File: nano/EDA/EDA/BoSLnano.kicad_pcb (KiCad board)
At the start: 4 copper layers, 74 x 30 mm, 59 parts, among them J1 Micro_SD_Card, J2 Conn_02x04_Counter_Clockwise, J3 Barrel_Jack_Switch, J4 USB_B_Micro, SW1 SPST, U1 MCP1700-3302E_SOT23, U10 FT232RQ, U2 ATmega328P-MMH, U3 MSQA6V1W5T2G, U4 NT3H2111W0FTT, U5 SIM7090, U6 74LV1T34GXH, U7 74LV1T34GXH, U8 MCP7940N-xSN, U9 74HC126PW-Q100, Y1 8 MHz, Y2 32.768 kHz

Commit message: finished bom and schematic - nano
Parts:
- removed BT1: Battery_Cell, SIMFootprints:2996TR
- removed D5, D6: LED, LED_SMD:LED_0603_1608Metric
- removed TP1: PWR_KEY, TestPoint:TestPoint_Pad_D1.0mm
- removed TP2: VDD_EXT, TestPoint:TestPoint_Pad_D1.0mm
- removed TP3: USB_DM, TestPoint:TestPoint_Pad_D1.0mm
- removed TP4: USB_DP, TestPoint:TestPoint_Pad_D1.0mm
- removed TP5: USB_VBUS, TestPoint:TestPoint_Pad_D1.0mm
- removed TP6: BOOT_CFG, TestPoint:TestPoint_Pad_D1.0mm
- removed U10: FT232RQ, Package_DFN_QFN:QFN-32-1EP_5x5mm_P0.5mm_EP3.1x3.1mm
- removed U7: 74LV1T34GXH, SIMFootprints:SOT1226
- removed U8: MCP7940N-xSN, Package_DFN_QFN:DFN-8-1EP_3x2mm_P0.5mm_EP1.3x1.5mm
- removed U9: 74HC126PW-Q100, Package_SO:TSSOP-14_4.4x5mm_P0.65mm
- removed Y2: 32.768 kHz, Crystal:Crystal_SMD_EuroQuartz_EQ161-2Pin_3.2x1.5mm
- added C13: 15 pF, Capacitor_SMD:C_0402_1005Metric, F.Cu at (133.2, 86.6)
- added C14: 1 μF, Capacitor_SMD:C_0402_1005Metric, F.Cu at (156.5, 94.6)
- added C15: 100 nF, Capacitor_SMD:C_0402_1005Metric, F.Cu at (128.7, 83.7)
- added C16: 15 pF, Capacitor_SMD:C_0402_1005Metric, F.Cu at (132.3, 97.1)
- added C17: 220 pF, Capacitor_SMD:C_0402_1005Metric, F.Cu at (135.2, 97.1)
- added C18: 100 nF, Capacitor_SMD:C_0402_1005Metric, F.Cu at (138.2, 95.6)
- added C19: 1 nF, Capacitor_SMD:C_0402_1005Metric, F.Cu at (150.8, 83.6)
- added J5: nRF_DBG, SIMFootprints:TC2030, F.Cu at (124.2, 80.6)
- added J6: Conn_01x10, Connector_PinHeader_2.54mm:PinHeader_1x10_P2.54mm_Vertical, F.Cu at (132.7, 60.4)
- added J7: Conn_01x04, Connector_PinHeader_2.54mm:PinHeader_1x04_P2.54mm_Vertical, F.Cu at (111.9, 75.6)
- added J8: Barrel_JACK, Connector_BarrelJack:BarrelJack_Horizontal, F.Cu at (175.0, 82.0)
- added J9: USB_B_Micro, Connector_USB:USB_Micro-B_Molex-105133-0001, F.Cu at (119.2, 75.9)
- added L1: 9.1 nH, Inductor_SMD:L_0603_1608Metric, F.Cu at (160.8, 93.9)
- added R11: 3.3 kΩ, Resistor_SMD:R_0402_1005Metric, F.Cu at (157.0, 91.7)
- added R12: 10 kΩ, Resistor_SMD:R_0402_1005Metric, F.Cu at (160.9, 97.4)
- added R13: 10 kΩ, Resistor_SMD:R_0402_1005Metric, F.Cu at (158.5, 94.6)
- added R14: 10 kΩ, Resistor_SMD:R_0402_1005Metric, F.Cu at (149.6, 89.6)
- added R15: 10 kΩ, Resistor_SMD:R_0402_1005Metric, F.Cu at (144.0, 95.0)
- AT1, AT2, D3: moved to F.Cu
- C1: value 0.1 μF -> 100 μF; footprint Capacitor_SMD:C_0805_2012Metric -> Capacitor_SMD:CP_Elec_5x5.8
- C10: value 12 pF -> 100 nF; footprint Capacitor_SMD:C_0603_1608Metric -> Capacitor_SMD:C_0402_1005Metric; moved to F.Cu
- C11, C12: footprint Capacitor_SMD:C_0603_1608Metric -> Capacitor_SMD:C_0402_1005Metric
- C2: value 1 μF -> 10 μF; footprint Capacitor_SMD:C_1206_3216Metric -> Capacitor_SMD:C_0805_2012Metric
- C3: value 330 μF -> 100 nF; footprint Capacitor_SMD:CP_Elec_8x10 -> Capacitor_SMD:C_0402_1005Metric
- C4: value 1 μF -> 15 pF; footprint Capacitor_SMD:C_1206_3216Metric -> Capacitor_SMD:C_0402_1005Metric
- C5: value 22 pF -> 15 pF; footprint Capacitor_SMD:C_0603_1608Metric -> Capacitor_SMD:C_0402_1005Metric; moved to F.Cu
- C6: value 22 pF -> 100 nF; footprint Capacitor_SMD:C_0603_1608Metric -> Capacitor_SMD:C_0402_1005Metric; moved to F.Cu
- C7: value 220 pF -> 100 nF; footprint Capacitor_SMD:C_0603_1608Metric -> Capacitor_SMD:C_0402_1005Metric; moved to F.Cu
- C8: value 33 pF -> 100 nF; footprint Capacitor_SMD:C_0603_1608Metric -> Capacitor_SMD:C_0402_1005Metric; moved to F.Cu
- C9: value 12 pF -> 1 μF; footprint Capacitor_SMD:C_0603_1608Metric -> Capacitor_SMD:C_0402_1005Metric; moved to F.Cu
- D1: value 1N4148 -> D_Schottky; footprint Diode_SMD:D_SOD-323 -> SIMFootprints:SOD882; moved to F.Cu
- J2: value Conn_02x04_Counter_Clockwise -> Conn_01x07; footprint Connector_PinHeader_2.54mm:PinHeader_2x04_P2.54mm_Vertical -> Connector_PinHeader_2.54mm:PinHeader_1x07_P2.54mm_Vertical
- J3: value Barrel_Jack_Switch -> Conn_01x04; footprint Connector_BarrelJack:BarrelJack_Horizontal -> Connector_PinHeader_2.54mm:PinHeader_1x04_P2.54mm_Vertical
- J4: value USB_B_Micro -> SAMD_DBG; footprint Connector_USB:USB_Micro-B_Molex-105133-0001 -> SIMFootprints:TC2030
- R1, R2: value 10 kΩ -> 1 kΩ; footprint Resistor_SMD:R_0603_1608Metric -> Resistor_SMD:R_0402_1005Metric; moved to F.Cu
- R10: footprint Resistor_SMD:R_0603_1608Metric -> Resistor_SMD:R_0402_1005Metric; moved to F.Cu
- R3: value 3.3 kΩ -> 39 Ω; footprint Resistor_SMD:R_0603_1608Metric -> Resistor_SMD:R_0402_1005Metric
- R4: value 3.3 kΩ -> 100 kΩ; footprint Resistor_SMD:R_0603_1608Metric -> Resistor_SMD:R_0402_1005Metric; moved to F.Cu
- R5, R6: value 10 kΩ -> 39 Ω; footprint Resistor_SMD:R_0603_1608Metric -> Resistor_SMD:R_0402_1005Metric; moved to F.Cu
- R7, R9: footprint Resistor_SMD:R_0603_1608Metric -> Resistor_SMD:R_0402_1005Metric
- R8: value 3.3 kΩ -> 10 kΩ; footprint Resistor_SMD:R_0603_1608Metric -> Resistor_SMD:R_0402_1005Metric
- U2: value ATmega328P-MMH -> ATSAMD21G18A-MUT; footprint Package_DFN_QFN:QFN-28-1EP_4x4mm_P0.45mm_EP2.4x2.4mm -> Package_DFN_QFN:QFN-48-1EP_7x7mm_P0.5mm_EP5.15x5.15mm; moved to F.Cu
- U3: value MSQA6V1W5T2G -> NT3H2111W0FTT; footprint Package_TO_SOT_SMD:SOT-353_SC-70-5 -> Package_SO:TSSOP-8_3x3mm_P0.65mm; moved to F.Cu
- U4: value NT3H2111W0FTT -> NRF9160; footprint Package_SO:TSSOP-8_3x3mm_P0.65mm -> SIMFootprints:nRF9160; moved to F.Cu
- U5: value SIM7090 -> BGA524N6; footprint SIMFootprints:SIM9000 -> SIMFootprints:TSNP-6-2; moved to F.Cu
- U6: value 74LV1T34GXH -> MSQA6V1W5T2G; footprint SIMFootprints:SOT1226 -> Package_TO_SOT_SMD:SOT-353_SC-70-5; moved to F.Cu
- Y1: value 8 MHz -> 32.768kHz; footprint Crystal:Crystal_SMD_EuroQuartz_MT-4Pin_3.2x2.5mm -> Crystal:Crystal_SMD_EuroQuartz_EQ161-2Pin_3.2x1.5mm; moved to F.Cu
- moved G1 62.0 mm to (37.0, 62.0), turned to 0 degrees
- moved J2 60.3 mm to (102.6, 75.6)
- moved H1 59.6 mm to (152.3, 79.6), turned to 0 degrees
- moved C7 59.4 mm to (163.7, 75.0), turned to 0 degrees
- moved R7 58.6 mm to (156.8, 81.0), turned to 0 degrees
- moved R8 57.8 mm to (156.8, 79.0)
- moved AE1 57.3 mm to (127.0, 75.0), turned to 0 degrees
- moved U3 54.2 mm to (152.8, 74.3), turned to 0 degrees
- moved C9 52.1 mm to (143.8, 91.1), turned to 0 degrees
- moved R5 51.1 mm to (152.6, 85.6), turned to 0 degrees
- moved J4 51.0 mm to (136.1, 86.0), turned to 0 degrees
- moved R10 50.0 mm to (159.7, 79.0), turned to 0 degrees
- moved R9 49.2 mm to (153.7, 83.6), turned to 0 degrees
- moved C11 49.2 mm to (149.6, 85.6), turned to 0 degrees
- moved R1 47.7 mm to (162.9, 97.6), turned to 270 degrees
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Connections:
- C10 pad 2: Net-(C10-Pad2) -> V_3.3
- C11 pad 1: GND -> V_3.3
- C11 pad 2: TTL_3.3V -> GND
- C12 pad 1: TLL_RST -> VPP
- C12 pad 2: Net-(C12-Pad2) -> GND
- C2 pad 1: VPP -> V_3.3
- C3 pad 1: VPP -> V_3.3
- C4 pad 1: V_3.3 -> Net-(C4-Pad1)
- C6 pad 1: GND -> RST
- C6 pad 2: Net-(C6-Pad2) -> GND
- C7 pad 1: GND -> V_3.3
- C7 pad 2: Net-(C7-Pad2) -> GND
- C8 pad 1: Net-(AT2-Pad1) -> V_3.3
- C8 pad 2: Net-(C8-Pad2) -> GND
- C9 pad 1: GND -> V_3.3
- C9 pad 2: Net-(C9-Pad2) -> GND
- D1 pad 1: ONOFF_PIN -> USB_ID
- D2 pad 2: Net-(D2-Pad2) -> USB_V
- D3 pad 2: Net-(D3-Pad2) -> nRF_STAT
- D4 pad 2: TTL_3.3V -> nRF_PWR
- I1 pad 1: Net-(C7-Pad2) -> Net-(C17-Pad2)
- J2 pad 5: D7 -> A4
- J2 pad 6: D6 -> A5
- J2 pad 7: D3 -> A6
- J3 pad 1: VPP -> V_3.3
- J3 pad 2: GND -> VPP
- J4 pad 1: USB_V -> V_3.3
- J4 pad 2: USB_DM -> SWDIO
- J4 pad 3: USB_DP -> Net-(J4-Pad3)
- J4 pad 4: Net-(J4-Pad4) -> SWCLK
- R1 pad 2: TLL_RST -> nRF_SWCLK
- R10 pad 1: Net-(D6-Pad1) -> Net-(D3-Pad1)
- R2 pad 2: NFC_I -> SWCLK
- R3 pad 1: Net-(D2-Pad1) -> Net-(J5-Pad6)
- R3 pad 2: GND -> nRF_EN
- R4 pad 1: Net-(D3-Pad1) -> V_3.3
- R4 pad 2: GND -> SD_CS
- R5 pad 1: SCL -> RST
- R5 pad 2: V_3.3 -> Net-(J4-Pad3)
- R6 pad 1: V_3.3 -> nRF_RST
- R6 pad 2: SDA -> Net-(J5-Pad3)
- R7 pad 1: TTL_3.3V -> RST
- R7 pad 2: GND -> V_3.3
- R8 pad 1: Net-(D4-Pad1) -> V_3.3
- R8 pad 2: Net-(R8-Pad2) -> NFC_I
- R9 pad 1: Net-(D5-Pad1) -> Net-(D2-Pad1)
- R9 pad 2: Net-(R9-Pad2) -> GND
- SW1 pad 2: TLL_RST -> RST
- U2 pad 1: D3 -> Net-(C4-Pad1)
- U2 pad 10: RX -> A4
- U2 pad 11: TX -> A5
- U2 pad 12: SD_CS -> A6
- U2 pad 13: SD_MOSI -> SDA
- U2 pad 14: SD_MISO -> SCL
- U2 pad 15: SD_SCLK -> D2
- U2 pad 16: V_3.3 -> D3
- U2 pad 17: AREF -> V_3.3
- U2 pad 19: A0 -> D4
- U2 pad 2: ONOFF_PIN -> Net-(C5-Pad2)
- U2 pad 20: A1 -> D5
- U2 pad 21: A2 -> SD_MOSI
- U2 pad 22: A3 -> SD_SCLK
- U2 pad 23: SDA -> SD_CS
- U2 pad 24: SCL -> SD_MISO
- U2 pad 25: TLL_RST -> D8
- U2 pad 26: TLL_RX -> D9
- U2 pad 27: TLL_TX -> Net-(D1-Pad2)
- U2 pad 28: D2 -> D10
- U2 pad 29: GND -> D6
- U2 pad 3: V_3.3 -> A0
- U2 pad 4: GND -> AREF
- U2 pad 5: Net-(C5-Pad2) -> GND
- U2 pad 6: Net-(C6-Pad2) -> V_3.3
- U2 pad 7: DTR -> VNFC
- U2 pad 8: D6 -> nRF_EN
- U2 pad 9: D7 -> A3
- U3 pad 1: Net-(I1-Pad3) -> Net-(AE1-Pad2)
- U3 pad 3: Net-(I1-Pad6) -> SCL
- U3 pad 4: Net-(I1-Pad2) -> NFC_I
- U3 pad 5: Net-(C7-Pad2) -> SDA
- U4 pad 1: Net-(AE1-Pad2) -> GND
- U4 pad 2: GND -> Net-(U4-Pad2)
- U4 pad 3: SCL -> nRF_STAT
- U4 pad 4: NFC_I -> nRF_PWR
- U4 pad 5: SDA -> GND
- U4 pad 6: VNFC -> GND
- U4 pad 7: Net-(U4-Pad7) -> GND
- U4 pad 8: Net-(AE1-Pad1) -> GND
- U5 pad 1: Net-(U5-Pad1) -> GND
- U5 pad 2: Net-(U5-Pad2) -> V_3.3
- U5 pad 3: Net-(U5-Pad3) -> Net-(U4-Pad67)
- U5 pad 4: Net-(U5-Pad4) -> GND
- U5 pad 6: Net-(U5-Pad6) -> Net-(U4-Pad93)
- U6 pad 1: (no net) -> Net-(I1-Pad2)
- U6 pad 2: TX -> GND
- U6 pad 3: GND -> Net-(I1-Pad3)
- U6 pad 4: Net-(U5-Pad6) -> Net-(I1-Pad6)
- U6 pad 5: V_1.8 -> Net-(C17-Pad2)
- Y1 pad 1: Net-(C6-Pad2) -> Net-(C4-Pad1)
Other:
- board size 74 x 30 mm -> 74 x 15 mm

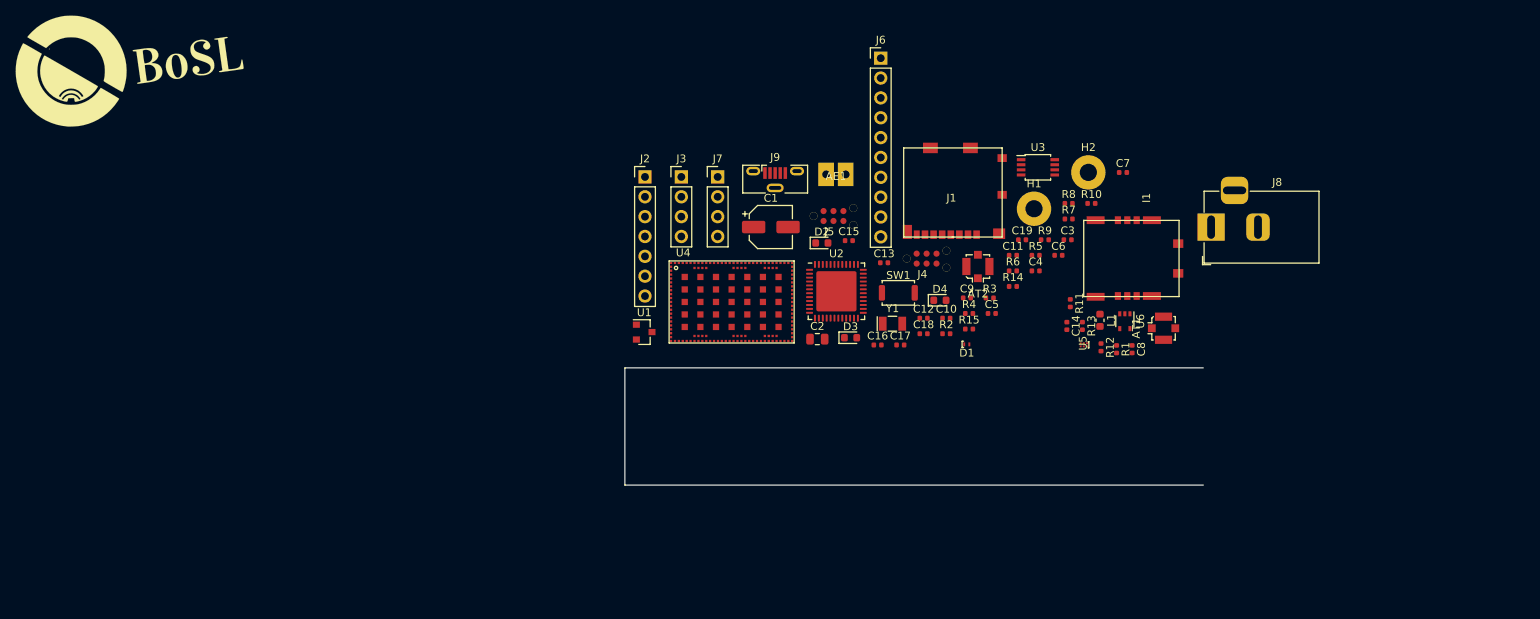
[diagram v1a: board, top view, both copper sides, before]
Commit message: added battery connector
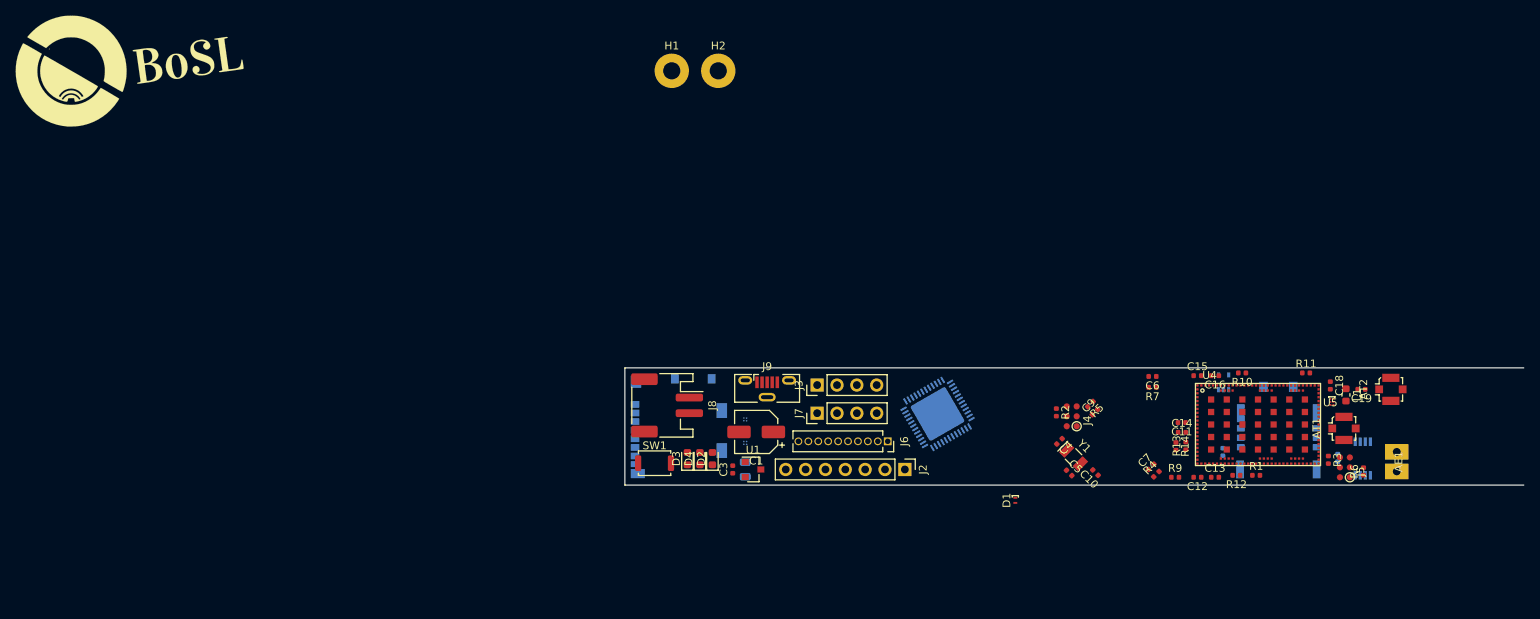
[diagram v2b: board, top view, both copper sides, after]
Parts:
- removed C8: 100 nF, Capacitor_SMD:C_0402_1005Metric
- removed R15: 10 kΩ, Resistor_SMD:R_0402_1005Metric
- added U7: MAX40203ANS, Package_BGA:WLP-4_0.73x0.73mm_Layout2x2_P0.35mm_Ball0.22mm_Pad0.2mm_NSMD, B.Cu at (115.4, 106.6)
- added U8: MAX40203ANS, Package_BGA:WLP-4_0.73x0.73mm_Layout2x2_P0.35mm_Ball0.22mm_Pad0.2mm_NSMD, B.Cu at (115.4, 109.6)
- C17, C2, I1, J1, R8, U2, U3, U6: moved to B.Cu
- J4, J5: footprint SIMFootprints:TC2030 -> SIMFootprints:TC2030_Pinless
- J6: footprint Connector_PinHeader_2.54mm:PinHeader_1x10_P2.54mm_Vertical -> Connector_PinSocket_1.27mm:PinSocket_1x10_P1.27mm_Vertical
- J8: value Barrel_JACK -> Jack-DC; footprint Connector_BarrelJack:BarrelJack_Horizontal -> Connector_JST:JST_PH_S2B-PH-SM4-TB_1x02-1MP_P2.00mm_Horizontal
- R14: value 10 kΩ -> 18 kΩ
- moved AE1 80.5 mm to (198.5, 112.0), turned to 90 degrees
- moved J5 76.3 mm to (192.1, 115.3), turned to 90 degrees
- moved J8 73.2 mm to (105.4, 104.8), turned to 270 degrees
- moved U4 69.1 mm to (181.0, 107.2)
- moved U3 55.8 mm to (194.4, 111.6), turned to 90 degrees
- moved AT2 55.1 mm to (198.0, 102.8), turned to 270 degrees
- moved C18 52.5 mm to (190.2, 102.2), turned to 270 degrees
- moved C3 52.0 mm to (113.8, 113.0), turned to 90 degrees
- moved R6 51.7 mm to (194.5, 113.2), turned to 90 degrees
- moved C13 50.5 mm to (175.5, 114.0)
- moved J2 50.1 mm to (135.8, 113.0), turned to 270 degrees
- moved H1 49.6 mm to (106.0, 62.0)
- moved H2 49.1 mm to (112.0, 62.0)
- moved J6 49.0 mm to (133.6, 109.4), turned to 270 degrees
- moved R3 48.0 mm to (190.0, 111.8), turned to 270 degrees
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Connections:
- AT1 pad 2: GND -> -BATT
- AT2 pad 2: GND -> -BATT
- C1 pad 2: GND -> -BATT
- C10 pad 1: GND -> -BATT
- C11 pad 2: GND -> -BATT
- C12 pad 2: GND -> -BATT
- C13 pad 2: GND -> -BATT
- C14 pad 1: GND -> -BATT
- C15 pad 1: GND -> -BATT
- C16 pad 1: GND -> -BATT
- C17 pad 1: GND -> -BATT
- C18 pad 1: GND -> -BATT
- C2 pad 2: GND -> -BATT
- C3 pad 2: GND -> -BATT
- C4 pad 2: GND -> -BATT
- C5 pad 1: GND -> -BATT
- C6 pad 2: GND -> -BATT
- C7 pad 2: GND -> -BATT
- C9 pad 2: GND -> -BATT
- I1 pad 4: GND -> -BATT
- J1 pad 6: GND -> -BATT
- J1 pad 9: GND -> -BATT
- J3 pad 3: GND -> -BATT
- J3 pad 4: GND -> -BATT
- J4 pad 5: GND -> -BATT
- J5 pad 5: GND -> -BATT
- J7 pad 2: GND -> -BATT
- J8 pad 1: VPP -> +BATT
- J8 pad 2: GND -> -BATT
- J9 pad 5: GND -> -BATT
- R10 pad 2: GND -> -BATT
- R11 pad 2: GND -> -BATT
- R14 pad 2: Net-(R14-Pad2) -> -BATT
- R8 pad 1: V_3.3 -> VNFC
- R9 pad 2: GND -> -BATT
- SW1 pad 1: GND -> -BATT
- U1 pad 1: GND -> -BATT
- U2 pad 18: GND -> -BATT
- U2 pad 35: GND -> -BATT
- U2 pad 42: GND -> -BATT
- U2 pad 5: GND -> -BATT
- U3 pad 2: GND -> -BATT
- U4 pad 1: GND -> -BATT
- U4 pad 103: GND -> -BATT
- U4 pad 11: GND -> -BATT
- U4 pad 14: GND -> -BATT
- U4 pad 17: GND -> -BATT
- U4 pad 21: GND -> -BATT
- U4 pad 27: GND -> -BATT
- U4 pad 3: nRF_STAT -> Net-(U4-Pad3)
- U4 pad 31: GND -> -BATT
- U4 pad 36: GND -> -BATT
- U4 pad 4: nRF_PWR -> Net-(U4-Pad4)
- U4 pad 41: GND -> -BATT
- U4 pad 44: GND -> -BATT
- U4 pad 47: GND -> -BATT
- U4 pad 5: GND -> -BATT
- U4 pad 50: GND -> -BATT
- U4 pad 52: GND -> -BATT
- U4 pad 56: GND -> -BATT
- U4 pad 6: GND -> -BATT
- U4 pad 60: GND -> -BATT
- U4 pad 62: GND -> -BATT
- U4 pad 63: GND -> -BATT
- U4 pad 65: GND -> -BATT
- U4 pad 66: GND -> -BATT
- U4 pad 68: GND -> -BATT
- U4 pad 69: GND -> -BATT
- U4 pad 7: GND -> -BATT
- U4 pad 72: GND -> -BATT
- U4 pad 74: GND -> -BATT
- U4 pad 75: GND -> -BATT
- U4 pad 76: GND -> -BATT
- U4 pad 77: GND -> -BATT
- U4 pad 78: GND -> -BATT
- U4 pad 79: GND -> -BATT
- U4 pad 8: GND -> -BATT
- U4 pad 80: GND -> -BATT
- U4 pad 81: GND -> -BATT
- U4 pad 82: GND -> -BATT
- U4 pad 83: Net-(U4-Pad83) -> nRF_PWR
- U4 pad 84: Net-(U4-Pad84) -> nRF_STAT
- U4 pad 85: GND -> -BATT
- U4 pad 9: GND -> -BATT
- U4 pad 90: GND -> -BATT
- U4 pad 94: GND -> -BATT
- U4 pad 98: GND -> -BATT
- U5 pad 1: GND -> -BATT
- U5 pad 4: GND -> -BATT
- U6 pad 2: GND -> -BATT
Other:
- board size 74 x 15 mm -> 115 x 15 mm

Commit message: modifed nano
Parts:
- removed G1: BoSL_Graphic, SIMFootprints:BoSL_Graphic
- removed H1, H2: MountingHole, MountingHole:MountingHole_2.2mm_M2_Pad
- C10, C4, C5, C7, C9, R4, Y1: moved to B.Cu
- moved C6 60.4 mm to (108.5, 114.0), turned to 0 degrees
- moved R9 59.7 mm to (111.6, 103.8), turned to 270 degrees
- moved R7 57.7 mm to (111.0, 114.0), turned to 0 degrees
- moved R4 47.4 mm to (121.2, 105.9), turned to 270 degrees
- moved R11 34.6 mm to (152.6, 100.8)
- moved C7 31.8 mm to (135.8, 108.8), turned to 120 degrees
- moved U4 31.8 mm to (149.2, 107.2)
- moved C12 31.6 mm to (141.7, 113.8)
- moved C13 31.6 mm to (143.9, 113.8)
- moved C15 31.6 mm to (141.7, 100.8)
- moved C16 31.6 mm to (143.9, 100.8)
- moved C19 31.6 mm to (162.6, 102.8)
- moved J5 31.6 mm to (160.5, 115.3)
- moved R12 31.6 mm to (146.6, 113.8)
- moved AE1 31.6 mm to (166.9, 112.0)
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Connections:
- D2 pad 1: Net-(D2-Pad1) -> -BATT
- D2 pad 2: USB_V -> Net-(D2-Pad2)
- D3 pad 1: Net-(D3-Pad1) -> -BATT
- D3 pad 2: nRF_STAT -> Net-(D3-Pad2)
- D4 pad 1: Net-(D4-Pad1) -> -BATT
- D4 pad 2: nRF_PWR -> Net-(D4-Pad2)
- R10 pad 1: Net-(D3-Pad1) -> nRF_STAT
- R10 pad 2: -BATT -> Net-(D3-Pad2)
- R11 pad 1: Net-(D4-Pad1) -> nRF_PWR
- R11 pad 2: -BATT -> Net-(D4-Pad2)
- R9 pad 1: Net-(D2-Pad1) -> USB_V
- R9 pad 2: -BATT -> Net-(D2-Pad2)
- U2 pad 49: (no net) -> -BATT
- U4 pad 15: Net-(R13-Pad2) -> Net-(U4-Pad15)
- U4 pad 42: Net-(U4-Pad42) -> Net-(R13-Pad2)
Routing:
- net VPP: track 0.00 -> 57.9 mm
- net SD_CS: track 0.00 -> 44.2 mm, vias 0 -> 2
- net SD_MISO: track 0.00 -> 37.0 mm, vias 0 -> 2
- net SD_MOSI: track 0.00 -> 34.2 mm, vias 0 -> 2
- net SD_SCLK: track 0.00 -> 32.6 mm, vias 0 -> 2
- net USB_DM: track 0.00 -> 31.1 mm, vias 0 -> 2
- net USB_DP: track 0.00 -> 30.7 mm, vias 0 -> 2
- net A6: track 0.00 -> 20.7 mm
- net A5: track 0.00 -> 19.7 mm
- net SWCLK: track 0.00 -> 19.6 mm, vias 0 -> 2
- net SWDIO: track 0.00 -> 19.6 mm, vias 0 -> 2
- net A2: track 0.00 -> 19.2 mm, vias 0 -> 1
- net A1: track 0.00 -> 19.2 mm, vias 0 -> 1
- net V_3.3: track 0.00 -> 18.5 mm, vias 0 -> 2
- net nRF_RST: track 0.00 -> 18.3 mm, vias 0 -> 2
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- added copper zone on In1.Cu, net -BATT
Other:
- board size 115 x 15 mm -> 69.2 x 15 mm
- net class Default: clearance 0.2 -> 0.16
- rule trace_clearance: 0.2 -> 0.16
- rule trace_min: 0.2 -> 0.1525
